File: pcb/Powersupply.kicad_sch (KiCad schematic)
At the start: 37 parts, among them IC3 UCC28910DR, Q3 HL3401A, U3 TPS54202DDC

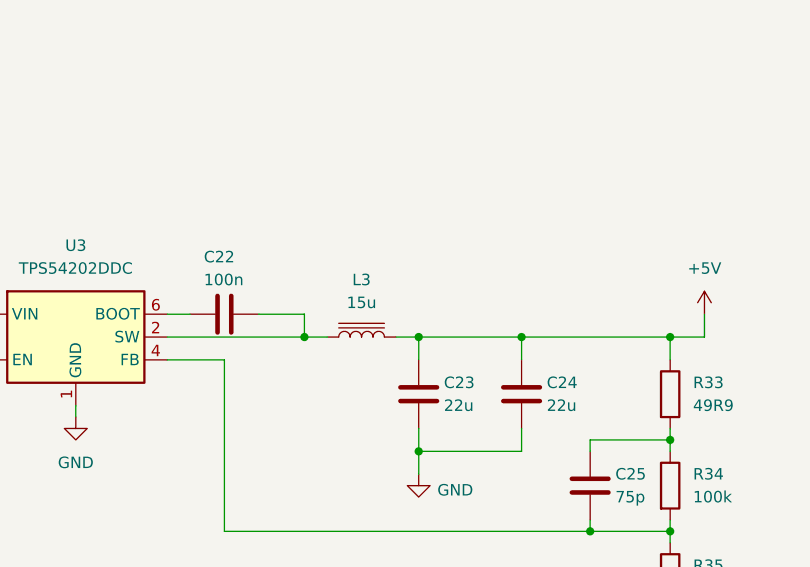
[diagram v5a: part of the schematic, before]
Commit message: added footprints
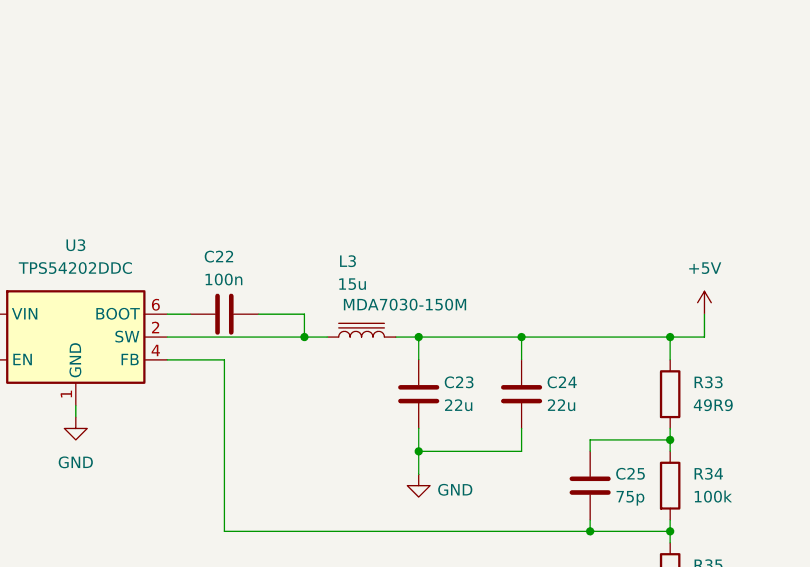
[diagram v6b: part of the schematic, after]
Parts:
- BR2: footprint SOP245P670X290-4N -> SamacSys_Parts:SOP245P670X290-4N
- C12: footprint (none) -> Capacitor_THT:C_Rect_L7.0mm_W2.0mm_P5.00mm
- C14: footprint (none) -> Capacitor_SMD:C_0201_0603Metric
- D8: footprint DIONM5436X261N -> SamacSys_Parts:DIONM5436X261N
- FB1: footprint BLM18SP221SN1B -> SamacSys_Parts:BLM18SP221SN1B
- IC3: footprint SOIC127P600X175-8N -> SamacSys_Parts:SOIC127P600X175-8N
- L3: footprint (none) -> Inductor_SMD:L_Coilcraft_XAL7030-152
- Q3: footprint (none) -> Package_TO_SOT_SMD:SOT-23
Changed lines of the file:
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@@
 			)
 		)
-		(property "Footprint" ""
+		(property "Footprint" "Package_TO_SOT_SMD:SOT-23"
 			(at 29.21 151.13 0)
 			(effects
@@
 			)
 		)
-		(property "Footprint" "SOIC127P600X175-8N"
+		(property "Footprint" "SamacSys_Parts:SOIC127P600X175-8N"
 			(at 119.38 83.82 0)
 			(effects
@@
 			)
 		)
-		(property "Footprint" "DIONM5436X261N"
+		(property "Footprint" "SamacSys_Parts:DIONM5436X261N"
 			(at 60.96 97.79 0)
 			(effects
@@
 			)
 		)
-		(property "Footprint" "BLM18SP221SN1B"
+		(property "Footprint" "SamacSys_Parts:BLM18SP221SN1B"
 			(at 257.81 25.4 0)
 			(effects
@@
 			)
 		)
-		(property "Footprint" ""
+		(property "Footprint" "Capacitor_SMD:C_0201_0603Metric"
 			(at 162.2552 77.47 0)
 			(effects
@@
 		(on_board yes)
 		(dnp no)
-		(fields_autoplaced yes)
 		(property "Reference" "L3"
-			(at 133.35 149.86 90)
+			(at 131.826 147.828 90)
 			(effects
 				(font
@@
 		)
 		(property "Value" "15u"
-			(at 133.35 152.4 90)
+			(at 132.334 150.368 90)
 			(effects
 				(font
@@
 			)
 		)
-		(property "Footprint" ""
+		(property "Footprint" "Inductor_SMD:L_Coilcraft_XAL7030-152"
 			(at 133.35 156.21 0)
 			(effects
@@
 			)
 		)
-		(property "Description" "Inductor with iron core"
-			(at 133.35 156.21 0)
+		(property "Description" "MDA7030-150M"
+			(at 138.176 152.654 90)
 			(effects
 				(font
 					(size 1.27 1.27)
 				)
-				(hide yes)
 			)
 		)
@@
 			)
 		)
-		(property "Footprint" "SOP245P670X290-4N"
+		(property "Footprint" "SamacSys_Parts:SOP245P670X290-4N"
 			(at 60.96 34.29 0)
 			(effects
@@
 			)
 		)
-		(property "Footprint" ""
+		(property "Footprint" "Capacitor_THT:C_Rect_L7.0mm_W2.0mm_P5.00mm"
 			(at 78.4352 99.06 0)
 			(effects

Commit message: fixed basic pcb errors
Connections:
- net +12V: now also Q3.3 (D); no longer Q3.D
- net at R36.1, R37.1: now also Q3.1 (G); no longer Q3.G
- net at C10.1, C20.1, C21.1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: now also Q3.2 (S); no longer Q3.S
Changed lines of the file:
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@@
 			)
 		)
-		(pin "D"
+		(pin "2"
 		)
-		(pin "S"
+		(pin "1"
 		)
-		(pin "G"
+		(pin "3"
 		)
 		(instances

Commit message: added connector and simulation link
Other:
- note added: "simulation"
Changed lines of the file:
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@@
+		)
+	)
+	(text "simulation"
+		(exclude_from_sim yes)
+		(at 56.134 18.542 0)
+		(effects
+			(font
+				(size 1.27 1.27)
+			)
+			(href "https://www.falstad.com/circuit/circuitjs.html?ctz=CQAgjCAMB0l3BWcMBMcUHYMGZIA4UA2ATmIxAUgpABZsKBTAWjDACgBncFPENX7NkJ98UMQDMAhgBsODNgDcQTPFRq8VVMISpaRfXGN3QEbAO7L1YzUfPLV1h1ch2b2qjf5RX2kRodeLhYswl5gPH7eACZ8CMLEwoLCviggUQxSAK7SAC5sMUngGMI0vgl8aRmS2XkFQuAlZaGVWbn5sfGJ9WDFFemteRaFvoW6dqPcvGND3b2FgXYocSDlS6F4U4vLPLwIxKk73halnRT7K8IuAE5nqeV7BxtilHDtTM6TYqn91W0A9uAQIQaGIaJBSCBsGgoNAIFRUj1vEA")
 		)
 	)
